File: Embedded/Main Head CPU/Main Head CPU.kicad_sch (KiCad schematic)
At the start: 52 parts, among them J1 10171746-00021LF, J10 Fan 1, J11 Substructure Power, J12 Head Power, J13 MicroSD, J14 Mic, J15 I2C, J2 LEDs 0, J3 LEDs 1, J4 LEDs 2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

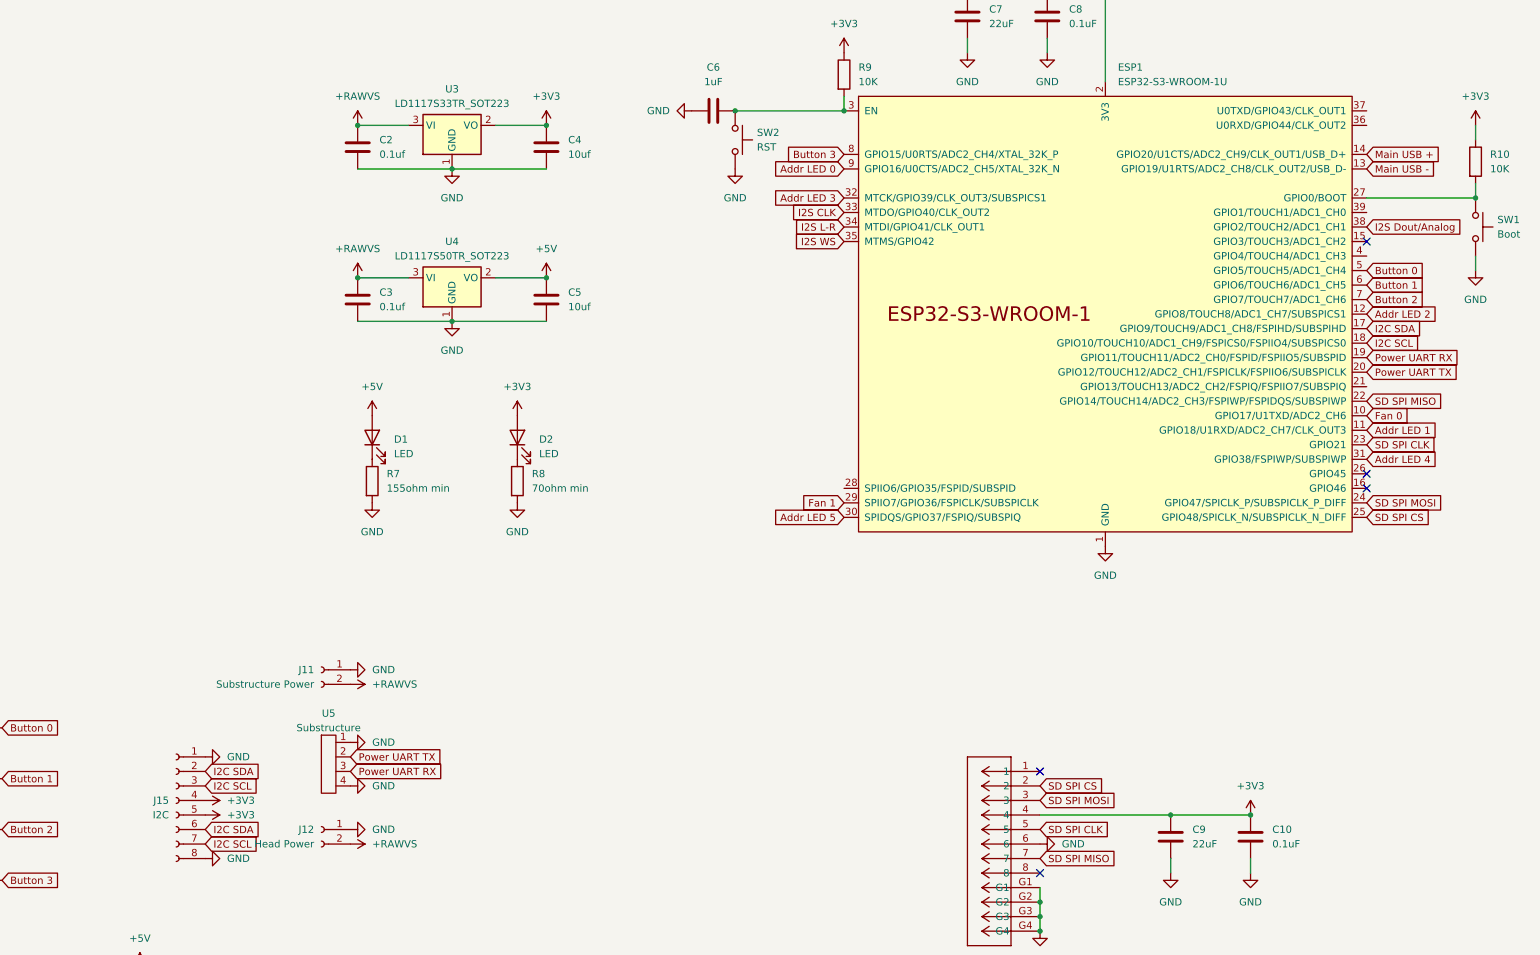
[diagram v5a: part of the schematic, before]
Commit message: Added UART Pins to Expansion
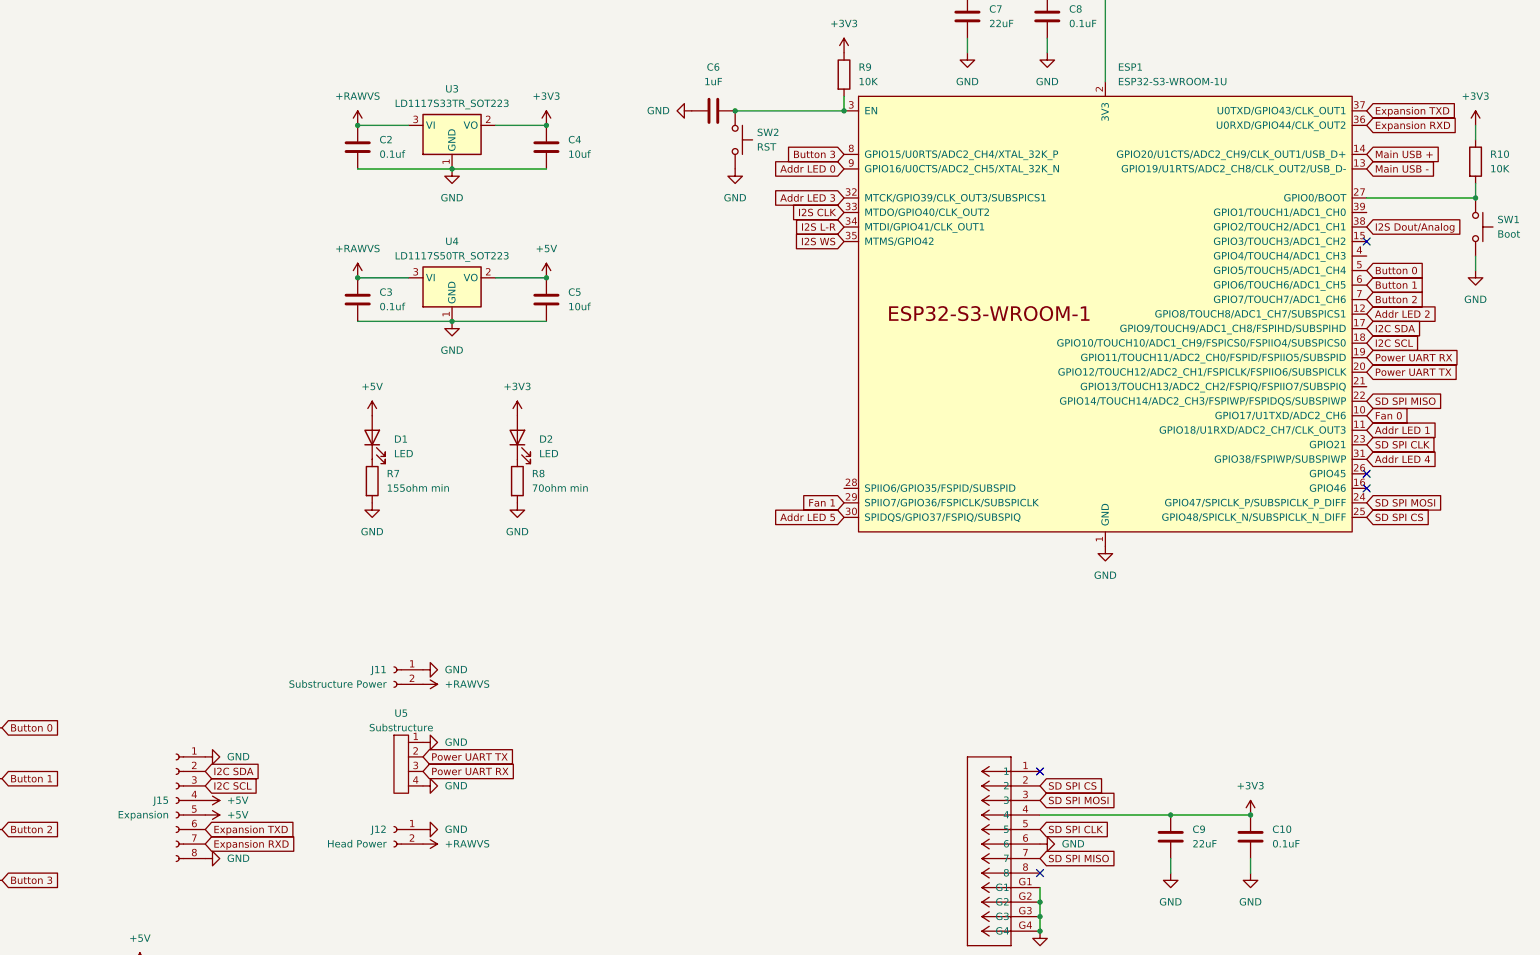
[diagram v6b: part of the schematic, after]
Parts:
- J15: value I2C -> Expansion
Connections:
- net +3V3: no longer J15.4 (Pin_4), J15.5 (Pin_5)
- net +5V: now also J15.4 (Pin_4), J15.5 (Pin_5)
- net I2C SCL: no longer J15.7 (Pin_7)
- net I2C SDA: no longer J15.6 (Pin_6)
- net Expansion RXD: now reaches ESP1.36 (U0RXD/GPIO44/CLK_OUT2)
- net Expansion RXD: now also J15.7 (Pin_7)
- net Expansion TXD: now reaches ESP1.37 (U0TXD/GPIO43/CLK_OUT1)
- net Expansion TXD: now also J15.6 (Pin_6)
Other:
- moved on the sheet: J11, J12, U5

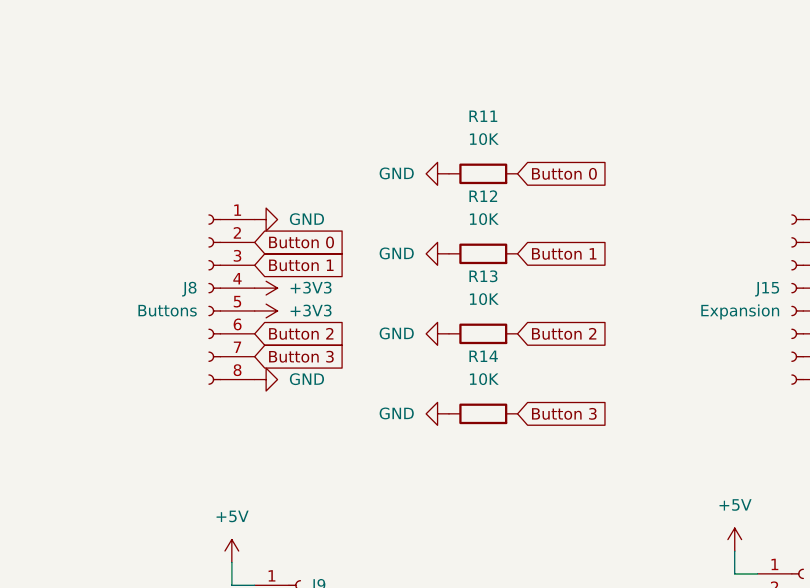
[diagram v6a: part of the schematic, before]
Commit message: Modified Buttons from pull down to pull up
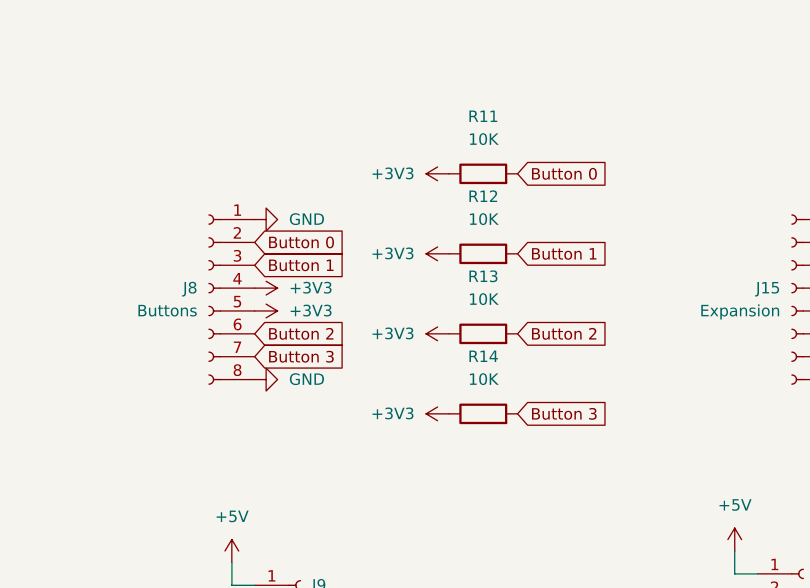
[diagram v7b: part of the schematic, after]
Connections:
- net +3V3: now also R11.1, R12.1, R13.1, R14.1
- net GND: no longer R11.1, R12.1, R13.1, R14.1
